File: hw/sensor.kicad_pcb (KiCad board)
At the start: 2 copper layers, 50 x 50 mm, 173 parts, among them P1 CONN_01X05, P2 CONN_01X03, P3 CONN_01X04, P4 CONN_01X05, SW1 DTSM-61N, U1 0868AT43A0020, U2 0896FB15A0100, U3 AT86RF212B, U4 ATSAML21E18B, U5 STLQ015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

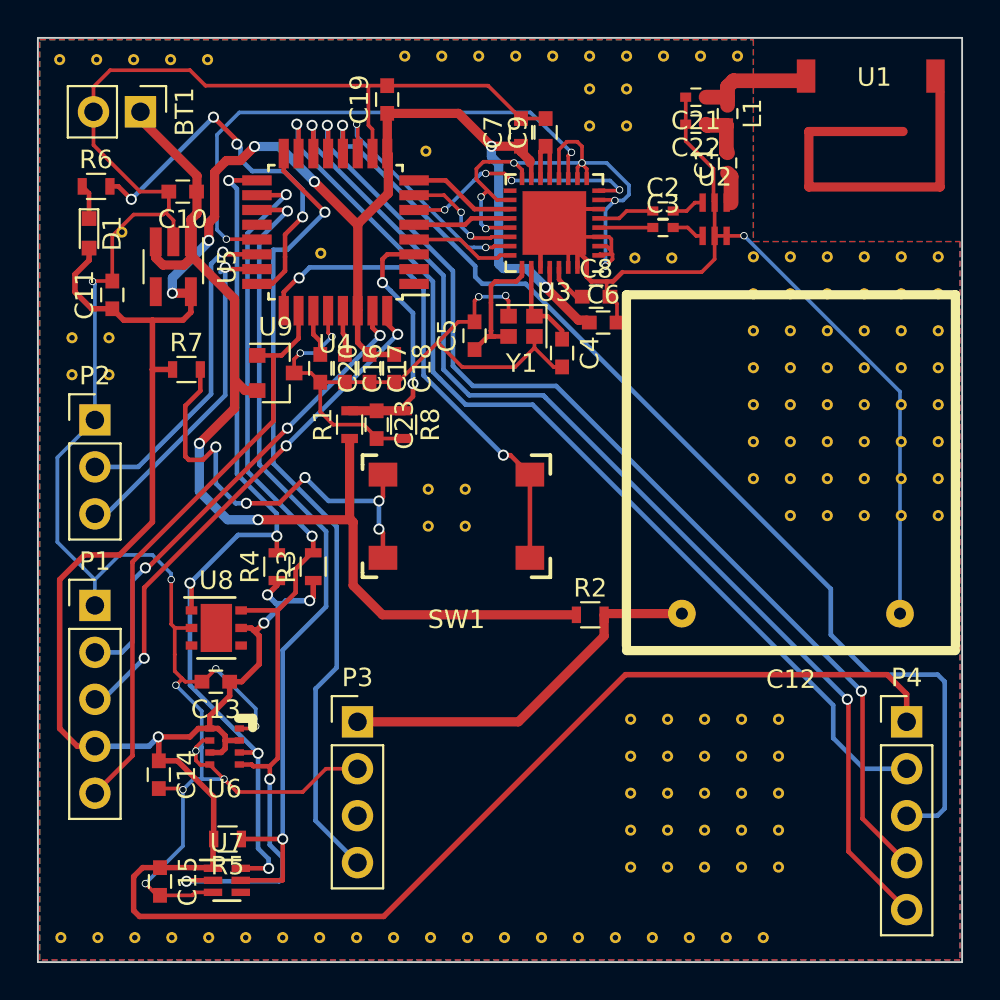
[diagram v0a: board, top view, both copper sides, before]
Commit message: fixed Supercap footprint, add more stiching, fixed uart to co2 sensor
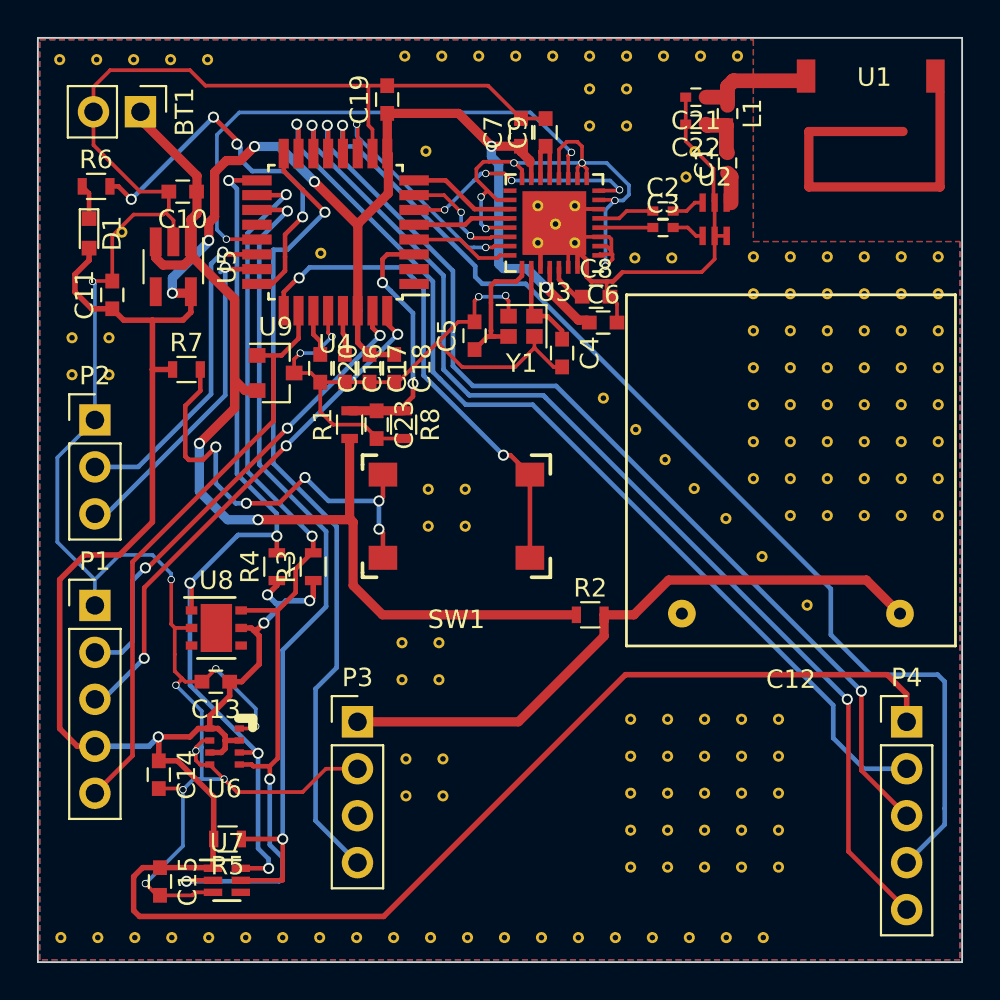
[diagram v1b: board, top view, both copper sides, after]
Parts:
- added REF**: STICH, custom:STICH, F.Cu at (170.5, 116.2)
- added REF**: STICH, custom:STICH, F.Cu at (154.9, 149.0)
- added REF**: STICH, custom:STICH, F.Cu at (176.6, 140.7)
- added REF**: STICH, custom:STICH, F.Cu at (174.2, 138.1)
- added REF**: STICH, custom:STICH, F.Cu at (172.2, 136.0)
- added REF**: STICH, custom:STICH, F.Cu at (170.5, 134.4)
- added REF**: STICH, custom:STICH, F.Cu at (168.9, 132.8)
- added REF**: STICH, custom:STICH, F.Cu at (167.3, 131.2)
- added REF**: STICH, custom:STICH, F.Cu at (165.6, 129.5)
- added REF**: STICH, custom:STICH, F.Cu at (163.0, 120.1)
- added REF**: STICH, custom:STICH, F.Cu at (164.0, 121.1)
- added REF**: STICH, custom:STICH, F.Cu at (170.1, 117.5)
- added REF**: STICH, custom:STICH, F.Cu at (162.0, 121.1)
- added REF**: STICH, custom:STICH, F.Cu at (164.0, 119.1)
- added REF**: STICH, custom:STICH, F.Cu at (162.0, 119.1)
- added REF**: STICH, custom:STICH, F.Cu at (156.7, 144.7)
- added REF**: STICH, custom:STICH, F.Cu at (154.7, 144.7)
- added REF**: STICH, custom:STICH, F.Cu at (156.7, 142.7)
- added REF**: STICH, custom:STICH, F.Cu at (154.7, 142.7)
- added REF**: STICH, custom:STICH, F.Cu at (156.9, 151.0)
- added REF**: STICH, custom:STICH, F.Cu at (154.9, 151.0)
- added REF**: STICH, custom:STICH, F.Cu at (156.9, 149.0)
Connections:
- P3 pad 3: (no net) -> Net-(P3-Pad3)
- U1 pad 2: (no net) -> Net-(U1-Pad2)
- U3 pad 17: (no net) -> Net-(U3-Pad17)
- U4 pad 1: (no net) -> Net-(U4-Pad1)
- U4 pad 12: /sensors/CO2_RXD -> /sensors/CO2_TXD
- U4 pad 13: /sensors/CO2_TXD -> /sensors/CO2_RXD
- U4 pad 2: (no net) -> Net-(U4-Pad2)
- U4 pad 20: (no net) -> Net-(U4-Pad20)
- U5 pad 4: (no net) -> Net-(U5-Pad4)
- U7 pad 4: (no net) -> Net-(U7-Pad4)
- U8 pad 3: (no net) -> Net-(U8-Pad3)
- U8 pad 4: (no net) -> Net-(U8-Pad4)
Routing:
- net GNDD: track 249.9 -> 225.0 mm, vias 20 -> 19
- net Net-(C12-Pad1): track 20.7 -> 34.0 mm
- net /sensors/CO2_RXD: track 58.1 -> 54.6 mm, vias 1 -> 2
- net /sensors/CO2_TXD: track 57.1 -> 59.7 mm, vias 2 -> 1
